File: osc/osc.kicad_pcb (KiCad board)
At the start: 2 copper layers, 25.4 x 25.4 mm, 23 parts, among them P1 CONN_1, P2 CONN_1, P3 CONN_1, P4 CONN_1, P5 CONN_1, P6 CONN_5X2, Y1 ASOF3S3, Y2 AOCJYR, Y3 AST3TQ-28, Y4 M100

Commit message: Ground connections and zone fill
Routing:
- net /GND: track 2.00 -> 19.6 mm, vias 0 -> 7
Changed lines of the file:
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@@
   (general
     (links 45)
-    (no_connects 19)
+    (no_connects 0)
     (area 99.924999 74.549999 126.725 101.05)
     (thickness 1.6)
     (drawings 8)
-    (tracks 80)
+    (tracks 98)
     (zones 0)
     (modules 23)
@@
   (layers
     (0 F.Cu signal)
-    (31 B.Cu signal hide)
+    (31 B.Cu signal)
     (32 B.Adhes user hide)
     (33 F.Adhes user)
@@
   )
   (setup
-    (last_trace_width 0.15)
+    (last_trace_width 0.4)
     (user_trace_width 0.15)
     (user_trace_width 0.2)
@@
     (user_trace_width 1.52)
     (trace_clearance 0.15)
-    (zone_clearance 0.5)
+    (zone_clearance 0.25)
     (zone_45_only no)
     (trace_min 0.15)
@@
     (pad_to_mask_clearance 0)
     (aux_axis_origin 100 100)
-    (visible_elements FFFF7F1F)
+    (visible_elements FFFFFF1F)
     (pcbplotparams
       (layerselection 0x00030_80000001)
@@
   (gr_line (start 125.4 98) (end 125.4 76.6) (angle 90) (layer Edge.Cuts) (width 0.1))
   (gr_line (start 100 100) (end 123.4 100) (angle 90) (layer Edge.Cuts) (width 0.1))
-  (segment (start 120.45 96.8) (end 120.45 94.9) (width 0.25) (layer F.Cu) (net 1) (status 400000))
-  (segment (start 119.86 94.31) (end 118.27 94.31) (width 0.25) (layer F.Cu) (net 1) (status 800000))
+  (segment (start 120.45 96.8) (end 120.45 94.9) (width 0.25) (layer F.Cu) (net 1))
+  (segment (start 119.86 94.31) (end 118.27 94.31) (width 0.25) (layer F.Cu) (net 1))
   (segment (start 120.45 94.9) (end 119.86 94.31) (width 0.25) (layer F.Cu) (net 1))
-  (segment (start 117.95 86.2) (end 119.1 86.2) (width 0.5) (layer F.Cu) (net 1) (status 400000))
+  (segment (start 117.95 86.2) (end 119.1 86.2) (width 0.5) (layer F.Cu) (net 1))
   (segment (start 119.7 91.1) (end 119.69 91.1) (width 0.5) (layer F.Cu) (net 1))
   (segment (start 119.7 86.8) (end 119.7 91.1) (width 0.5) (layer F.Cu) (net 1))
   (segment (start 119.1 86.2) (end 119.7 86.8) (width 0.5) (layer F.Cu) (net 1))
-  (segment (start 123.5 91.1) (end 121 91.1) (width 1) (layer F.Cu) (net 1) (status 400000))
+  (segment (start 123.5 91.1) (end 121 91.1) (width 1) (layer F.Cu) (net 1))
   (segment (start 121 91.1) (end 121.05 91.05) (width 1) (layer F.Cu) (net 1))
-  (segment (start 119 79.14) (end 121.05 81.19) (width 1) (layer F.Cu) (net 1) (status 400000))
+  (segment (start 119 79.14) (end 121.05 81.19) (width 1) (layer F.Cu) (net 1))
   (segment (start 121.05 91.05) (end 121 91.1) (width 1) (layer F.Cu) (net 1))
   (segment (start 121.05 81.19) (end 121.05 91.05) (width 1) (layer F.Cu) (net 1))
   (segment (start 121 91.1) (end 119.69 91.1) (width 0.5) (layer F.Cu) (net 1))
   (segment (start 119.69 91.1) (end 118.27 92.52) (width 0.5) (layer F.Cu) (net 1))
-  (segment (start 105.87 91.345) (end 105.875 91.35) (width 0.5) (layer F.Cu) (net 1) (status C00000))
-  (segment (start 105.875 91.35) (end 117.1 91.35) (width 0.5) (layer F.Cu) (net 1) (status 400000))
-  (segment (start 118.27 92.52) (end 118.27 94.31) (width 0.5) (layer F.Cu) (net 1) (status 800000))
+  (segment (start 105.87 91.345) (end 105.875 91.35) (width 0.5) (layer F.Cu) (net 1))
+  (segment (start 105.875 91.35) (end 117.1 91.35) (width 0.5) (layer F.Cu) (net 1))
+  (segment (start 118.27 92.52) (end 118.27 94.31) (width 0.5) (layer F.Cu) (net 1))
   (segment (start 117.1 91.35) (end 118.27 92.52) (width 0.5) (layer F.Cu) (net 1))
-  (segment (start 105.85 93.55) (end 105.87 93.53) (width 0.5) (layer F.Cu) (net 1) (status C00000))
-  (segment (start 105.87 93.53) (end 105.87 91.345) (width 0.5) (layer F.Cu) (net 1) (status C00000))
-  (segment (start 115.49 86.2) (end 117.95 86.2) (width 0.4) (layer F.Cu) (net 1) (status C00000))
+  (segment (start 105.85 93.55) (end 105.87 93.53) (width 0.5) (layer F.Cu) (net 1))
+  (segment (start 105.87 93.53) (end 105.87 91.345) (width 0.5) (layer F.Cu) (net 1))
+  (segment (start 115.49 86.2) (end 117.95 86.2) (width 0.4) (layer F.Cu) (net 1))
   (segment (start 119 79.14) (end 119 79.15) (width 1) (layer F.Cu) (net 1))
   (segment (start 115.05 93.75) (end 115.05 93.8) (width 0.5) (layer F.Cu) (net 1))
@@
   (segment (start 116.84 94.31) (end 118.27 94.31) (width 0.5) (layer F.Cu) (net 1))
   (segment (start 116.2 94.95) (end 116.84 94.31) (width 0.5) (layer F.Cu) (net 1))
-  (segment (start 114.7 96.8) (end 112.7 96.8) (width 0.5) (layer F.Cu) (net 2) (status C00000))
+  (segment (start 117.95 84.7) (end 119.4 84.7) (width 0.4) (layer F.Cu) (net 2))
+  (via (at 119.4 84.7) (size 0.6) (drill 0.25) (layers F.Cu B.Cu) (net 2))
+  (segment (start 109.05 89.75) (end 107.5 89.75) (width 1) (layer F.Cu) (net 2))
+  (via (at 107.5 89.75) (size 0.6) (drill 0.25) (layers F.Cu B.Cu) (net 2))
+  (segment (start 107.35 93.55) (end 107.35 92.65) (width 0.4) (layer F.Cu) (net 2))
+  (via (at 107.35 92.65) (size 0.6) (drill 0.25) (layers F.Cu B.Cu) (net 2))
+  (segment (start 102.03 88.855) (end 102.03 87.12) (width 1) (layer F.Cu) (net 2))
+  (via (at 102.05 87.1) (size 0.6) (drill 0.25) (layers F.Cu B.Cu) (net 2))
+  (segment (start 102.03 87.12) (end 102.05 87.1) (width 1) (layer F.Cu) (net 2))
+  (segment (start 105.25 82.19) (end 105.25 83.65) (width 1) (layer F.Cu) (net 2))
+  (via (at 105.25 83.65) (size 0.6) (drill 0.25) (layers F.Cu B.Cu) (net 2))
+  (segment (start 103.03 82.19) (end 105.25 82.19) (width 1) (layer F.Cu) (net 2))
+  (segment (start 105.25 82.19) (end 110.4 82.19) (width 1) (layer F.Cu) (net 2))
+  (segment (start 110.4 82.19) (end 110.41 82.2) (width 1) (layer F.Cu) (net 2))
+  (segment (start 123.5 88.1) (end 123.5 86.6) (width 0.5) (layer F.Cu) (net 2))
+  (via (at 123.5 86.6) (size 0.6) (drill 0.25) (layers F.Cu B.Cu) (net 2))
+  (segment (start 124.3 94.6) (end 124.3 93.05) (width 0.5) (layer F.Cu) (net 2))
+  (via (at 124.3 93.05) (size 0.6) (drill 0.25) (layers F.Cu B.Cu) (net 2))
+  (segment (start 114.7 96.8) (end 112.7 96.8) (width 0.5) (layer F.Cu) (net 2))
   (segment (start 109.05 93.75) (end 106 96.8) (width 0.15) (layer F.Cu) (net 4))
   (segment (start 106 96.8) (end 103.2 96.8) (width 0.15) (layer F.Cu) (net 4))
@@
   (segment (start 106.3 80.45) (end 106.3 79.14) (width 1) (layer B.Cu) (net 11))
   (segment (start 105.4 81.35) (end 106.3 80.45) (width 1) (layer B.Cu) (net 11))
-  (segment (start 118.27 82.19) (end 115.5 82.19) (width 0.15) (layer F.Cu) (net 12) (status C00000))
-  (segment (start 115.5 82.19) (end 114.71 82.19) (width 0.15) (layer F.Cu) (net 12) (status 400000))
+  (segment (start 118.27 82.19) (end 115.5 82.19) (width 0.15) (layer F.Cu) (net 12))
+  (segment (start 115.5 82.19) (end 114.71 82.19) (width 0.15) (layer F.Cu) (net 12))
   (segment (start 114.71 82.19) (end 112.25 84.65) (width 0.15) (layer F.Cu) (net 12))
   (segment (start 118.25 98.75) (end 102.5 98.75) (width 0.15) (layer F.Cu) (net 12))
@@
   (segment (start 113.5 88.2) (end 107.75 88.2) (width 0.15) (layer F.Cu) (net 12))
   (zone (net 2) (net_name /GND) (layer B.Cu) (hatch edge 0.508)
-    (connect_pads yes (clearance 0.5))
-    (min_thickness 0.2)
-    (fill (arc_segments 16) (thermal_gap 0.5) (thermal_bridge_width 0.5) (smoothing chamfer) (radius 0.25))
+    (connect_pads (clearance 0.25))
+    (min_thickness 0.15)
+    (fill yes (arc_segments 16) (thermal_gap 0.5) (thermal_bridge_width 0.5) (smoothing chamfer) (radius 0.25))
     (polygon
       (pts
@@
     (connect_pads yes (clearance 0.5))
     (min_thickness 0.2)
-    (fill (arc_segments 16) (thermal_gap 0.5) (thermal_bridge_width 0.5) (smoothing chamfer) (radius 0.25))
+    (fill yes (arc_segments 16) (thermal_gap 0.5) (thermal_bridge_width 0.5) (smoothing chamfer) (radius 0.25))
     (polygon
       (pts

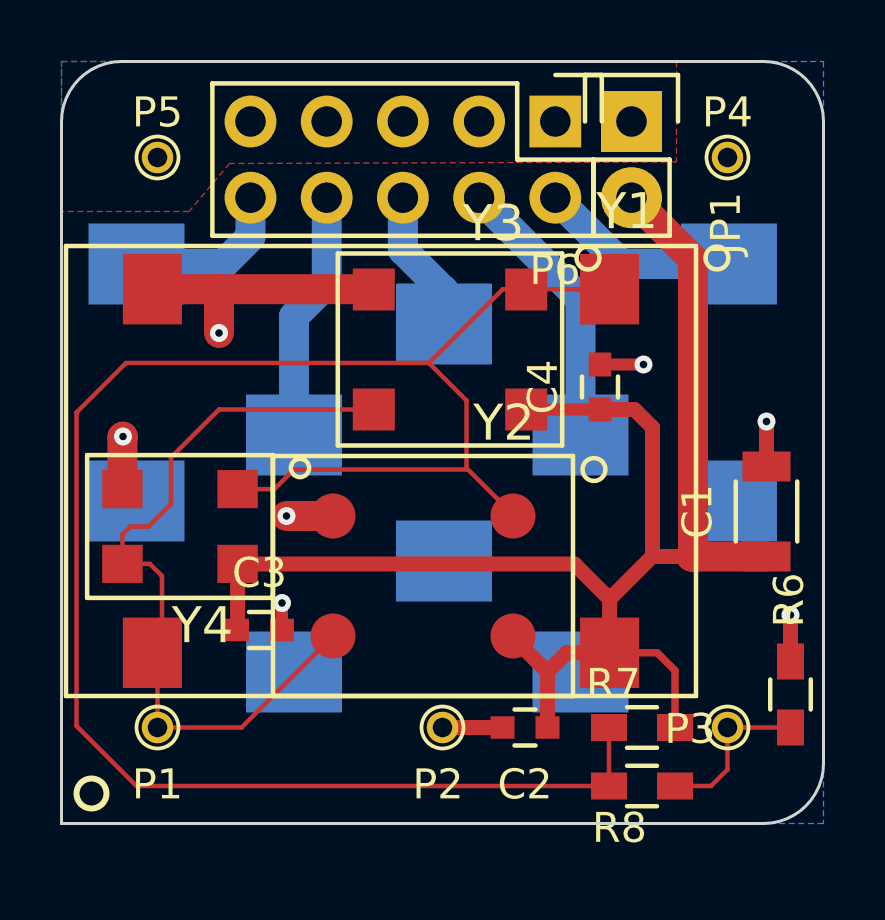
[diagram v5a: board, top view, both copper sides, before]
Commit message: Remove ref.designators, add net labels for external signals.
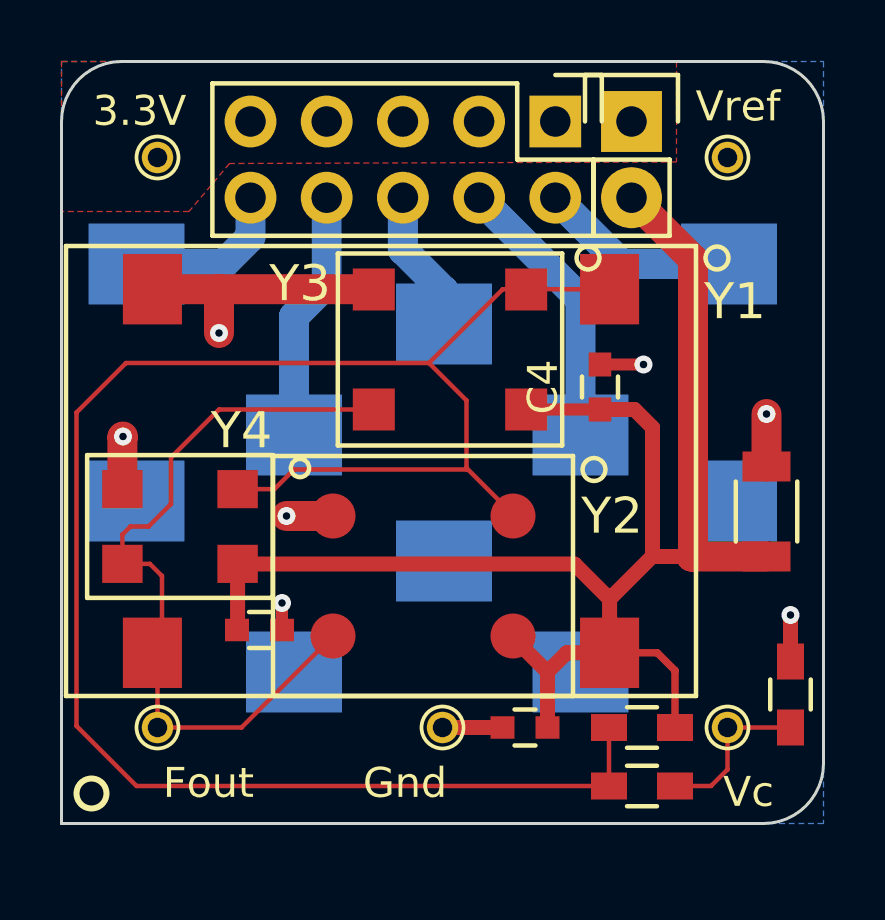
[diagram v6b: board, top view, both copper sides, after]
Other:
- board text added: "3.3V"
- board text added: "Fout"
- board text added: "Gnd"
- board text added: "Vc"
- board text added: "Vref"
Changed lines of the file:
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@@
     (area 99.924999 74.549999 126.725 101.05)
     (thickness 1.6)
-    (drawings 8)
+    (drawings 13)
     (tracks 98)
     (zones 0)
@@
   )
   (setup
-    (last_trace_width 0.4)
+    (last_trace_width 1)
     (user_trace_width 0.15)
     (user_trace_width 0.2)
@@
     (mod_text_size 1 1)
     (mod_text_width 0.15)
-    (pad_size 1.7272 1.7272)
-    (pad_drill 1.016)
+    (pad_size 1.05 1.05)
+    (pad_drill 0.65)
     (pad_to_mask_clearance 0)
     (aux_axis_origin 100 100)
-    (visible_elements FFFFFF1F)
+    (visible_elements FFFFFF7F)
     (pcbplotparams
       (layerselection 0x00030_80000001)
@@
     (descr "Through hole pin header")
     (tags "pin header")
-    (fp_text reference JP1 (at 3.15 3.4 90) (layer F.SilkS)
+    (fp_text reference JP1 (at 3.15 3.4 90) (layer F.SilkS) hide
       (effects (font (size 1 1) (thickness 0.1)))
     )
@@
     (descr "Through hole pin header")
     (tags "pin header")
-    (fp_text reference P6 (at 4.95 0.01 360) (layer F.SilkS)
+    (fp_text reference P6 (at 4.95 0.01 360) (layer F.SilkS) hide
       (effects (font (size 1 1) (thickness 0.1)))
     )
@@
     (tags "resistor 0603")
     (attr smd)
-    (fp_text reference R6 (at -3.15 0.05 270) (layer F.SilkS)
+    (fp_text reference R6 (at -1.1 1.6 270) (layer F.SilkS) hide
       (effects (font (size 1 1) (thickness 0.1)))
     )
@@
     (tags "resistor 0603")
     (attr smd)
-    (fp_text reference R7 (at -0.95 -1.45) (layer F.SilkS)
+    (fp_text reference R7 (at -0.95 -1.45) (layer F.SilkS) hide
       (effects (font (size 1 1) (thickness 0.1)))
     )
@@
     (tags "resistor 0603")
     (attr smd)
-    (fp_text reference R8 (at 0.75 -1.4 180) (layer F.SilkS)
+    (fp_text reference R8 (at 0.75 -1.4 180) (layer F.SilkS) hide
       (effects (font (size 1 1) (thickness 0.1)))
     )
@@
     (descr "module 1 pin (ou trou mecanique de percage)")
     (tags DEV)
-    (fp_text reference P1 (at 0 1.9) (layer F.SilkS)
+    (fp_text reference P1 (at 0 1.9) (layer F.SilkS) hide
       (effects (font (size 1 1) (thickness 0.1)))
     )
@@
     (descr "module 1 pin (ou trou mecanique de percage)")
     (tags DEV)
-    (fp_text reference P2 (at -0.15 1.9) (layer F.SilkS)
+    (fp_text reference P2 (at -0.15 1.9) (layer F.SilkS) hide
       (effects (font (size 1 1) (thickness 0.1)))
     )
@@
     (descr "module 1 pin (ou trou mecanique de percage)")
     (tags DEV)
-    (fp_text reference P3 (at -1.25 0.05) (layer F.SilkS)
+    (fp_text reference P3 (at -1.25 0.05) (layer F.SilkS) hide
       (effects (font (size 1 1) (thickness 0.1)))
     )
@@
     (descr "module 1 pin (ou trou mecanique de percage)")
     (tags DEV)
-    (fp_text reference P4 (at 0 -1.5) (layer F.SilkS)
+    (fp_text reference P4 (at 0 -1.5) (layer F.SilkS) hide
       (effects (font (size 1 1) (thickness 0.1)))
     )
@@
     (descr "module 1 pin (ou trou mecanique de percage)")
     (tags DEV)
-    (fp_text reference P5 (at 0 -1.5) (layer F.SilkS)
+    (fp_text reference P5 (at 0 -1.5) (layer F.SilkS) hide
       (effects (font (size 1 1) (thickness 0.1)))
     )
@@
   (module footprints:OSC5032 (layer F.Cu)
     (at 103.95 90.1 180)
-    (fp_text reference Y4 (at -0.75 -3.3 360) (layer F.SilkS)
+    (fp_text reference Y4 (at -2.05 3.2 360) (layer F.SilkS)
       (effects (font (size 1.2 1.2) (thickness 0.15)))
     )
@@
   (module footprints:OSC7050 (layer F.Cu)
     (at 112.95 84.2 180)
-    (fp_text reference Y3 (at -1.45 4.2 360) (layer F.SilkS)
+    (fp_text reference Y3 (at 5 2.2 360) (layer F.SilkS)
       (effects (font (size 1.2 1.2) (thickness 0.15)))
     )
@@
   (module footprints:OSC-ASOF3S3 (layer F.Cu)
     (at 110.65 88.25 180)
-    (fp_text reference Y1 (at -8.2 8.65 360) (layer F.SilkS)
+    (fp_text reference Y1 (at -11.8 5.65 360) (layer F.SilkS)
       (effects (font (size 1.2 1.2) (thickness 0.15)))
     )
@@
   (module footprints:OSC-AOCJYR-SMT (layer F.Cu)
     (at 112.05 91.75 180)
-    (fp_text reference Y2 (at -2.7 5.1 180) (layer F.SilkS)
+    (fp_text reference Y2 (at -6.3 2 180) (layer F.SilkS)
       (effects (font (size 1.2 1.2) (thickness 0.15)))
     )
@@
     (tags "capacitor 1206")
     (attr smd)
-    (fp_text reference C1 (at 0 -2.3 90) (layer F.SilkS)
+    (fp_text reference C1 (at 3.35 -0.05 90) (layer F.SilkS) hide
       (effects (font (size 1 1) (thickness 0.15)))
     )
@@
     (tags "capacitor 0603")
     (attr smd)
-    (fp_text reference C2 (at 0 -1.9 180) (layer F.SilkS)
+    (fp_text reference C2 (at 0 -1.9 180) (layer F.SilkS) hide
       (effects (font (size 1 1) (thickness 0.15)))
     )
@@
     (tags "capacitor 0603")
     (attr smd)
-    (fp_text reference C3 (at 0 -1.9) (layer F.SilkS)
+    (fp_text reference C3 (at -0.9 1.5) (layer F.SilkS) hide
       (effects (font (size 1 1) (thickness 0.15)))
     )
@@
       (effects (font (size 1 1) (thickness 0.15)))
     )
-    (fp_text value 0.1uF (at 0 1.9 90) (layer F.Fab)
+    (fp_text value 0.1uF (at 0 1.9 90) (layer F.Fab) hide
       (effects (font (size 1 1) (thickness 0.15)))
     )
@@
       (rotate (xyz 0 0 0))
     )
+  )
+  (gr_text Vref (at 122.55 76.1) (layer F.SilkS)
+    (effects (font (size 1 1) (thickness 0.15)))
+  )
+  (gr_text 3.3V (at 102.6 76.25) (layer F.SilkS)
+    (effects (font (size 1 1) (thickness 0.15)))
+  )
+  (gr_text Vc (at 122.9 98.95) (layer F.SilkS)
+    (effects (font (size 1 1) (thickness 0.15)))
+  )
+  (gr_text Gnd (at 111.45 98.65) (layer F.SilkS)
+    (effects (font (size 1 1) (thickness 0.15)))
+  )
+  (gr_text Fout (at 104.9 98.65) (layer F.SilkS)
+    (effects (font (size 1 1) (thickness 0.15)))
   )
   (gr_circle (center 101 99) (end 101 99.5) (layer F.SilkS) (width 0.2))
@@
   (segment (start 116.84 94.31) (end 118.27 94.31) (width 0.5) (layer F.Cu) (net 1))
   (segment (start 116.2 94.95) (end 116.84 94.31) (width 0.5) (layer F.Cu) (net 1))
+  (segment (start 123.5 88.1) (end 123.5 86.35) (width 1) (layer F.Cu) (net 2))
+  (via (at 123.5 86.35) (size 0.6) (drill 0.25) (layers F.Cu B.Cu) (net 2))
   (segment (start 117.95 84.7) (end 119.4 84.7) (width 0.4) (layer F.Cu) (net 2))
   (via (at 119.4 84.7) (size 0.6) (drill 0.25) (layers F.Cu B.Cu) (net 2))
@@
   (segment (start 105.25 82.19) (end 110.4 82.19) (width 1) (layer F.Cu) (net 2))
   (segment (start 110.4 82.19) (end 110.41 82.2) (width 1) (layer F.Cu) (net 2))
-  (segment (start 123.5 88.1) (end 123.5 86.6) (width 0.5) (layer F.Cu) (net 2))
-  (via (at 123.5 86.6) (size 0.6) (drill 0.25) (layers F.Cu B.Cu) (net 2))
   (segment (start 124.3 94.6) (end 124.3 93.05) (width 0.5) (layer F.Cu) (net 2))
   (via (at 124.3 93.05) (size 0.6) (drill 0.25) (layers F.Cu B.Cu) (net 2))

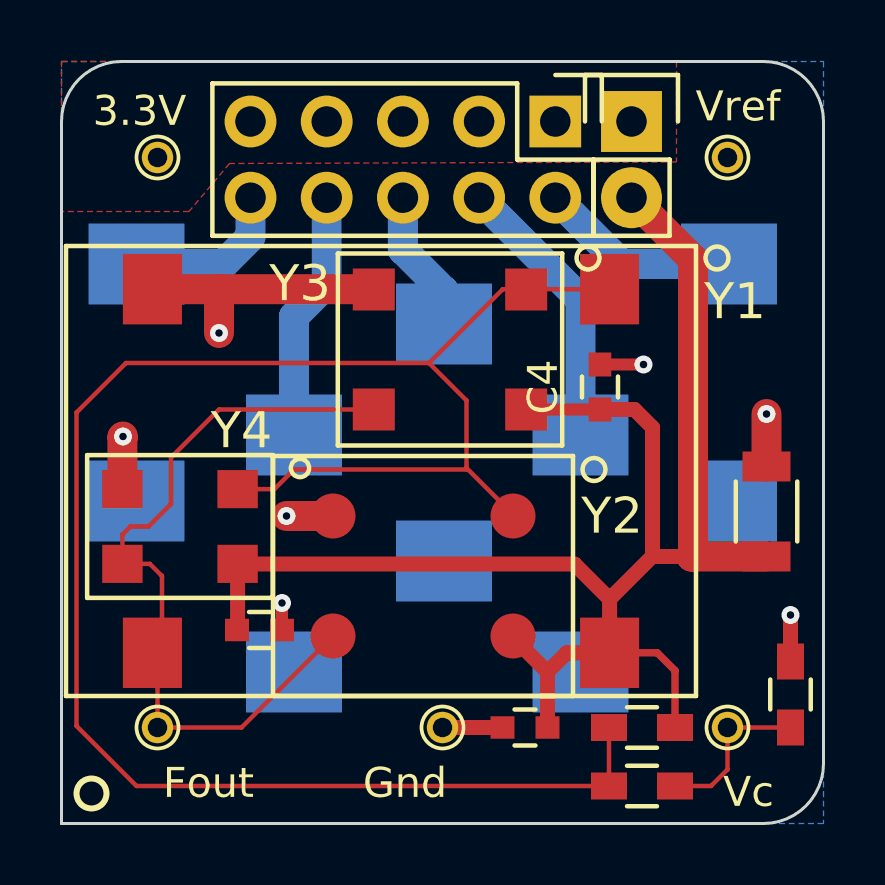
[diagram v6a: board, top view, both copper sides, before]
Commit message: Refactor oscillator board before releasing to manufacturing: trace width, combine headers to a single part, etc.
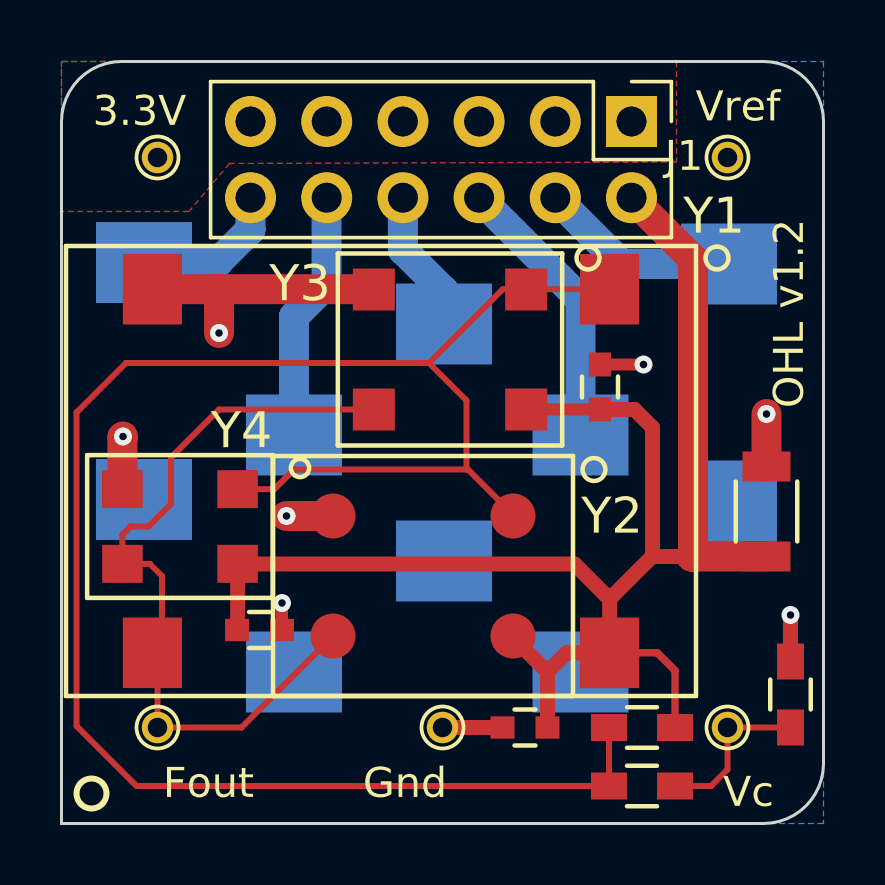
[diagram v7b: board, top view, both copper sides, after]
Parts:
- removed JP1: JUMPER, Pin_Headers:Pin_Header_Straight_1x02
- removed P6: CONN_5X2, Pin_Headers:Pin_Header_Straight_2x05
- added J1: CONN_02X06, Pin_Headers:Pin_Header_Straight_2x06_Pitch2.54mm, F.Cu at (119.0, 76.6)
- moved R1 0.25 mm to (102.8, 85.2)
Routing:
- net /Fout: track 27.2 -> 25.9 mm
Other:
- net class Default: clearance 0.15 -> 0.2; trace_width 0.15 -> 0.2; via_drill 0.25 -> 0.3
- rule trace_clearance: 0.15 -> 0.2
- rule trace_min: 0.15 -> 0.2
- board text added: "OHL v1.2"
